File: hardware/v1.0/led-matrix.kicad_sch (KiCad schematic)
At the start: 93 parts, among them J1 Conn_01x01, J10 Conn_01x01, J11 Conn_01x01, J12 Conn_01x01, J2 Conn_01x01, J3 Conn_01x01, J4 Conn_01x01, J5 Conn_01x01, J6 Conn_01x01, J7 Conn_01x01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

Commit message: hardware done.
- update pcb.

Signed-off-by: UnsicentificLaLaLaLa <zhaohao1997@foxmail.com>
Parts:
- R1, R2, R3, R4, R5, R6, R7, R8: value 1K -> 2K
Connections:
- net PA13: now also D16.1 (K), D24.1 (K), D32.1 (K), D40.1 (K), D48.1 (K), D56.1 (K), D64.1 (K), D8.1 (K); no longer D14.1 (K), D22.1 (K), D30.1 (K), D38.1 (K), D46.1 (K), D54.1 (K), D6.1 (K), D62.1 (K)
- net PA14: now also D15.1 (K), D23.1 (K), D31.1 (K), D39.1 (K), D47.1 (K), D55.1 (K), D63.1 (K), D7.1 (K); no longer D13.1 (K), D21.1 (K), D29.1 (K), D37.1 (K), D45.1 (K), D5.1 (K), D53.1 (K), D61.1 (K)
- net PA15: now also D13.1 (K), D21.1 (K), D29.1 (K), D37.1 (K), D45.1 (K), D5.1 (K), D53.1 (K), D61.1 (K); no longer D15.1 (K), D23.1 (K), D31.1 (K), D39.1 (K), D47.1 (K), D55.1 (K), D63.1 (K), D7.1 (K)
- net PA2: now also D14.1 (K), D22.1 (K), D30.1 (K), D38.1 (K), D46.1 (K), D54.1 (K), D6.1 (K), D62.1 (K); no longer D16.1 (K), D24.1 (K), D32.1 (K), D40.1 (K), D48.1 (K), D56.1 (K), D64.1 (K), D8.1 (K)
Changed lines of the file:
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@@
     (effects (font (size 1.27 1.27)) (justify right bottom))
   )
-  (label "PA14" (at 148.59 50.8 0) (fields_autoplaced)
+  (label "PA14" (at 173.99 50.8 0) (fields_autoplaced)
     (effects (font (size 1.27 1.27)) (justify left bottom))
   )
@@
     (effects (font (size 1.27 1.27)) (justify right bottom))
   )
-  (label "PA15" (at 173.99 50.8 0) (fields_autoplaced)
+  (label "PA15" (at 148.59 50.8 0) (fields_autoplaced)
     (effects (font (size 1.27 1.27)) (justify left bottom))
   )
@@
     (effects (font (size 1.27 1.27)) (justify right bottom))
   )
-  (label "PA13" (at 161.29 50.8 0) (fields_autoplaced)
+  (label "PA13" (at 186.69 50.8 0) (fields_autoplaced)
     (effects (font (size 1.27 1.27)) (justify left bottom))
   )
@@
     (effects (font (size 1.27 1.27)) (justify right bottom))
   )
-  (label "PA2" (at 186.69 50.8 0) (fields_autoplaced)
+  (label "PA2" (at 161.29 50.8 0) (fields_autoplaced)
     (effects (font (size 1.27 1.27)) (justify left bottom))
   )
@@
       (effects (font (size 1.27 1.27)))
     )
-    (property "Value" "1K" (at 203.2 82.55 90)
+    (property "Value" "2K" (at 203.2 82.55 90)
       (effects (font (size 1.27 1.27)))
     )
@@
       (effects (font (size 1.27 1.27)))
     )
-    (property "Value" "1K" (at 203.2 146.05 90)
+    (property "Value" "2K" (at 203.2 146.05 90)
       (effects (font (size 1.27 1.27)))
     )
@@
       (effects (font (size 1.27 1.27)))
     )
-    (property "Value" "1K" (at 203.2 120.65 90)
+    (property "Value" "2K" (at 203.2 120.65 90)
       (effects (font (size 1.27 1.27)))
     )
@@
       (effects (font (size 1.27 1.27)))
     )
-    (property "Value" "1K" (at 203.2 133.35 90)
+    (property "Value" "2K" (at 203.2 133.35 90)
       (effects (font (size 1.27 1.27)))
     )
@@
       (effects (font (size 1.27 1.27)))
     )
-    (property "Value" "1K" (at 203.2 95.25 90)
+    (property "Value" "2K" (at 203.2 95.25 90)
       (effects (font (size 1.27 1.27)))
     )
@@
       (effects (font (size 1.27 1.27)))
     )
-    (property "Value" "1K" (at 203.2 69.85 90)
+    (property "Value" "2K" (at 203.2 69.85 90)
       (effects (font (size 1.27 1.27)))
     )
@@
       (effects (font (size 1.27 1.27)))
     )
-    (property "Value" "1K" (at 203.2 57.15 90)
+    (property "Value" "2K" (at 203.2 57.15 90)
       (effects (font (size 1.27 1.27)))
     )
@@
       (effects (font (size 1.27 1.27)))
     )
-    (property "Value" "1K" (at 203.2 107.95 90)
-      (effects (font (size 1.27 1.27)))
-    )
+    (property "Value" "2K" (at 203.2 107.95 90)
+      (effects (font (size 1.27 1.27)))
+    )

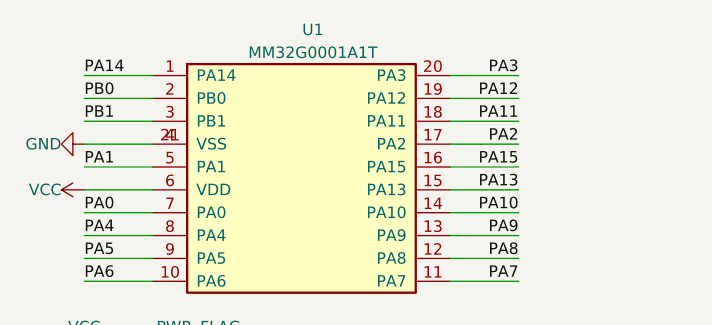
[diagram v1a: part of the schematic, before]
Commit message: add production.
- add prd.
- update pcb file.

Signed-off-by: zhaohao <zhaohao@mindmotion.com.cn>
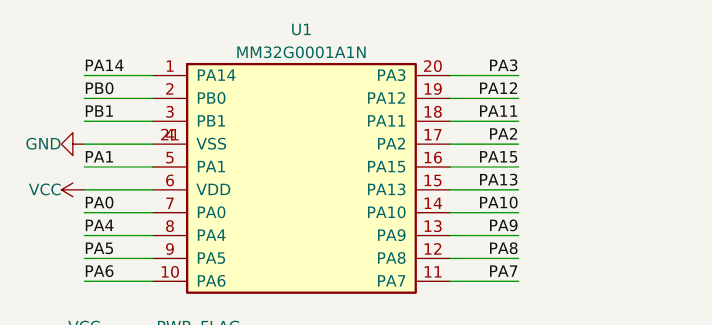
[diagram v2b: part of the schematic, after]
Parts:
- U1: value MM32G0001A1T -> MM32G0001A1N
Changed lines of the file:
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@@
   (symbol (lib_id "Connector_Generic:Conn_02x10_Counter_Clockwise") (at 49.53 50.8 0) (unit 1)
     (in_bom yes) (on_board yes) (dnp no) (fields_autoplaced)
-    (property "Reference" "U1" (at 50.8 35.56 0)
+    (property "Reference" "U1" (at 49.53 35.56 0)
       (effects (font (size 1.27 1.27)))
     )
-    (property "Value" "MM32G0001A1T" (at 50.8 38.1 0)
+    (property "Value" "MM32G0001A1N" (at 49.53 38.1 0)
       (effects (font (size 1.27 1.27)))
     )
